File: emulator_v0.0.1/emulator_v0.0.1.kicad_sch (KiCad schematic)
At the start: 11 parts, among them J1 Conn_01x10_Socket, J2 Conn_01x05_Pin, U1 L7805

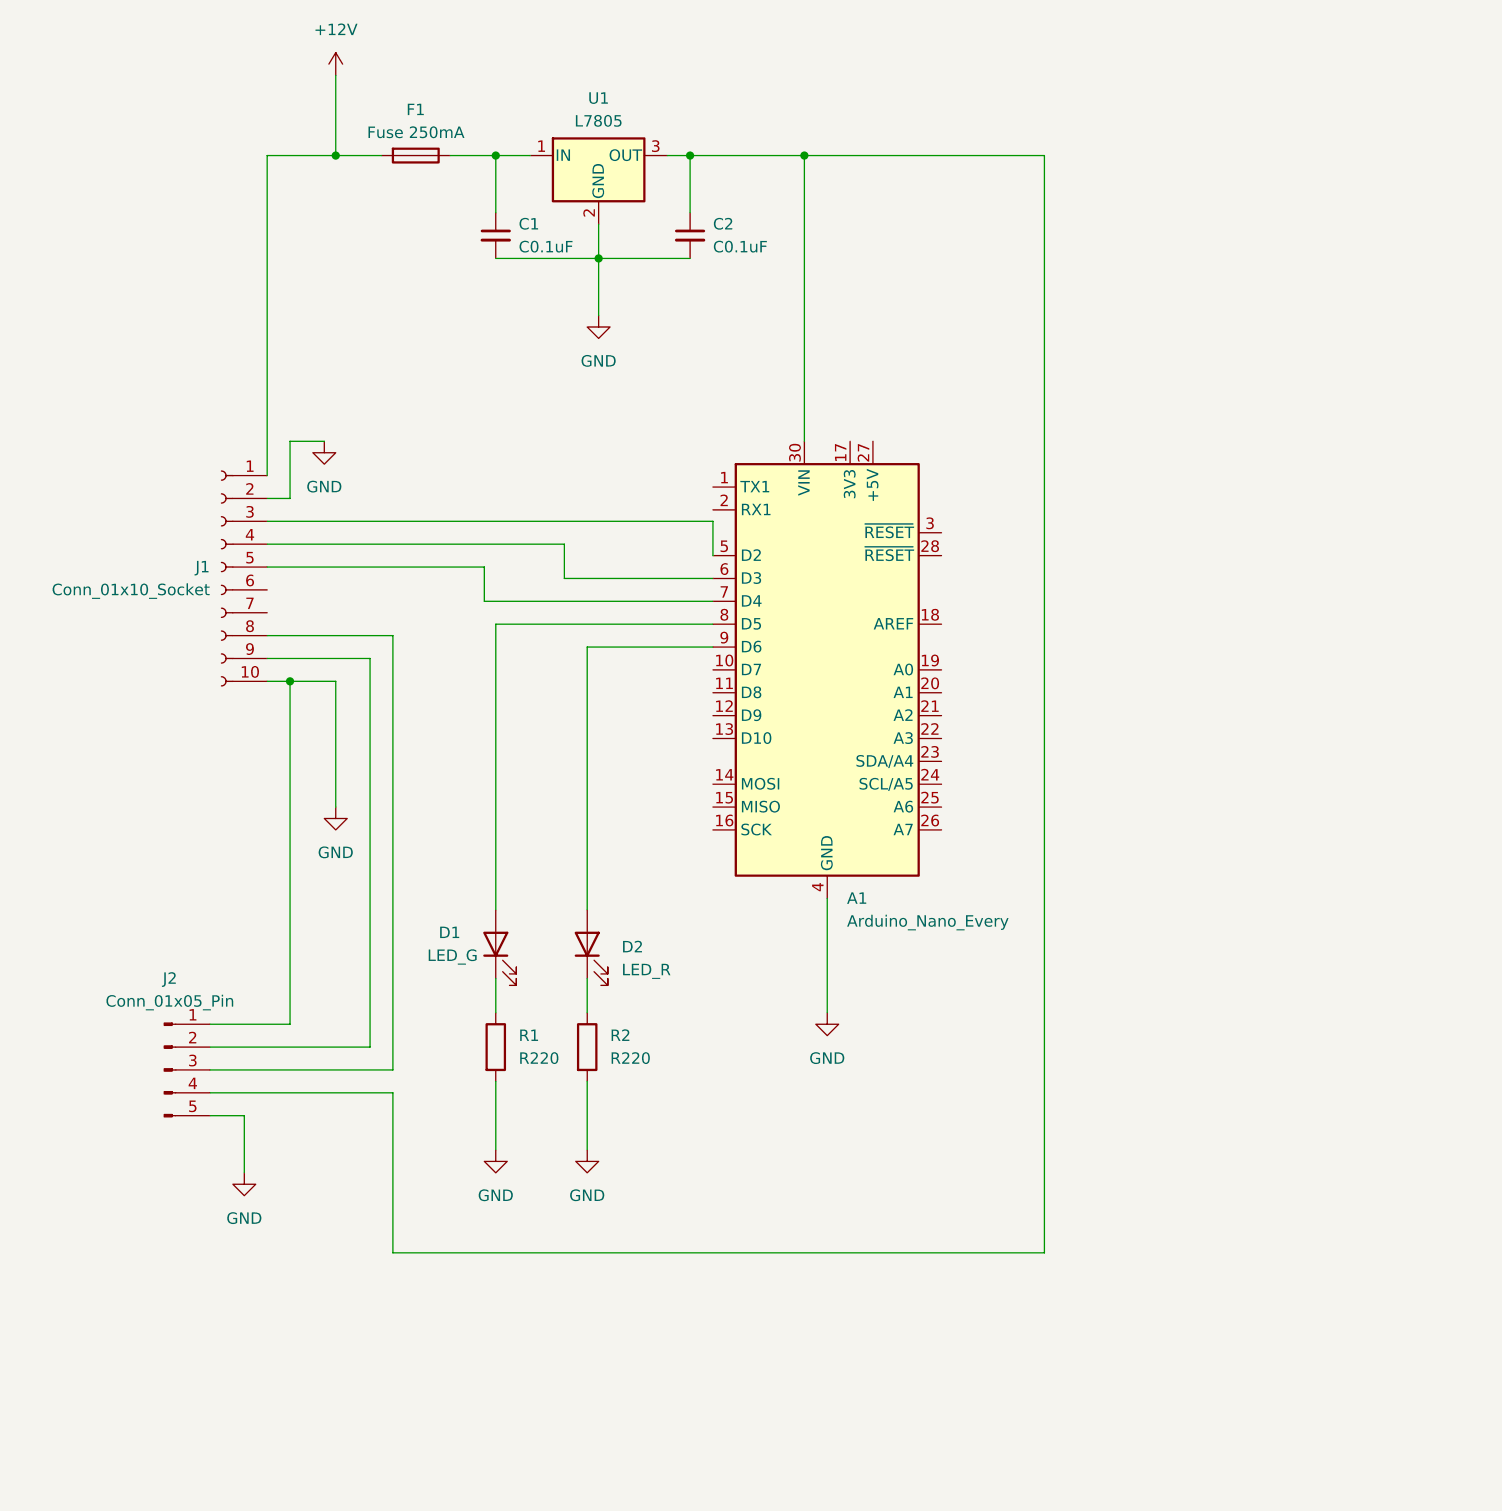
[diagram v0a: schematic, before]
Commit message: added control for powering up
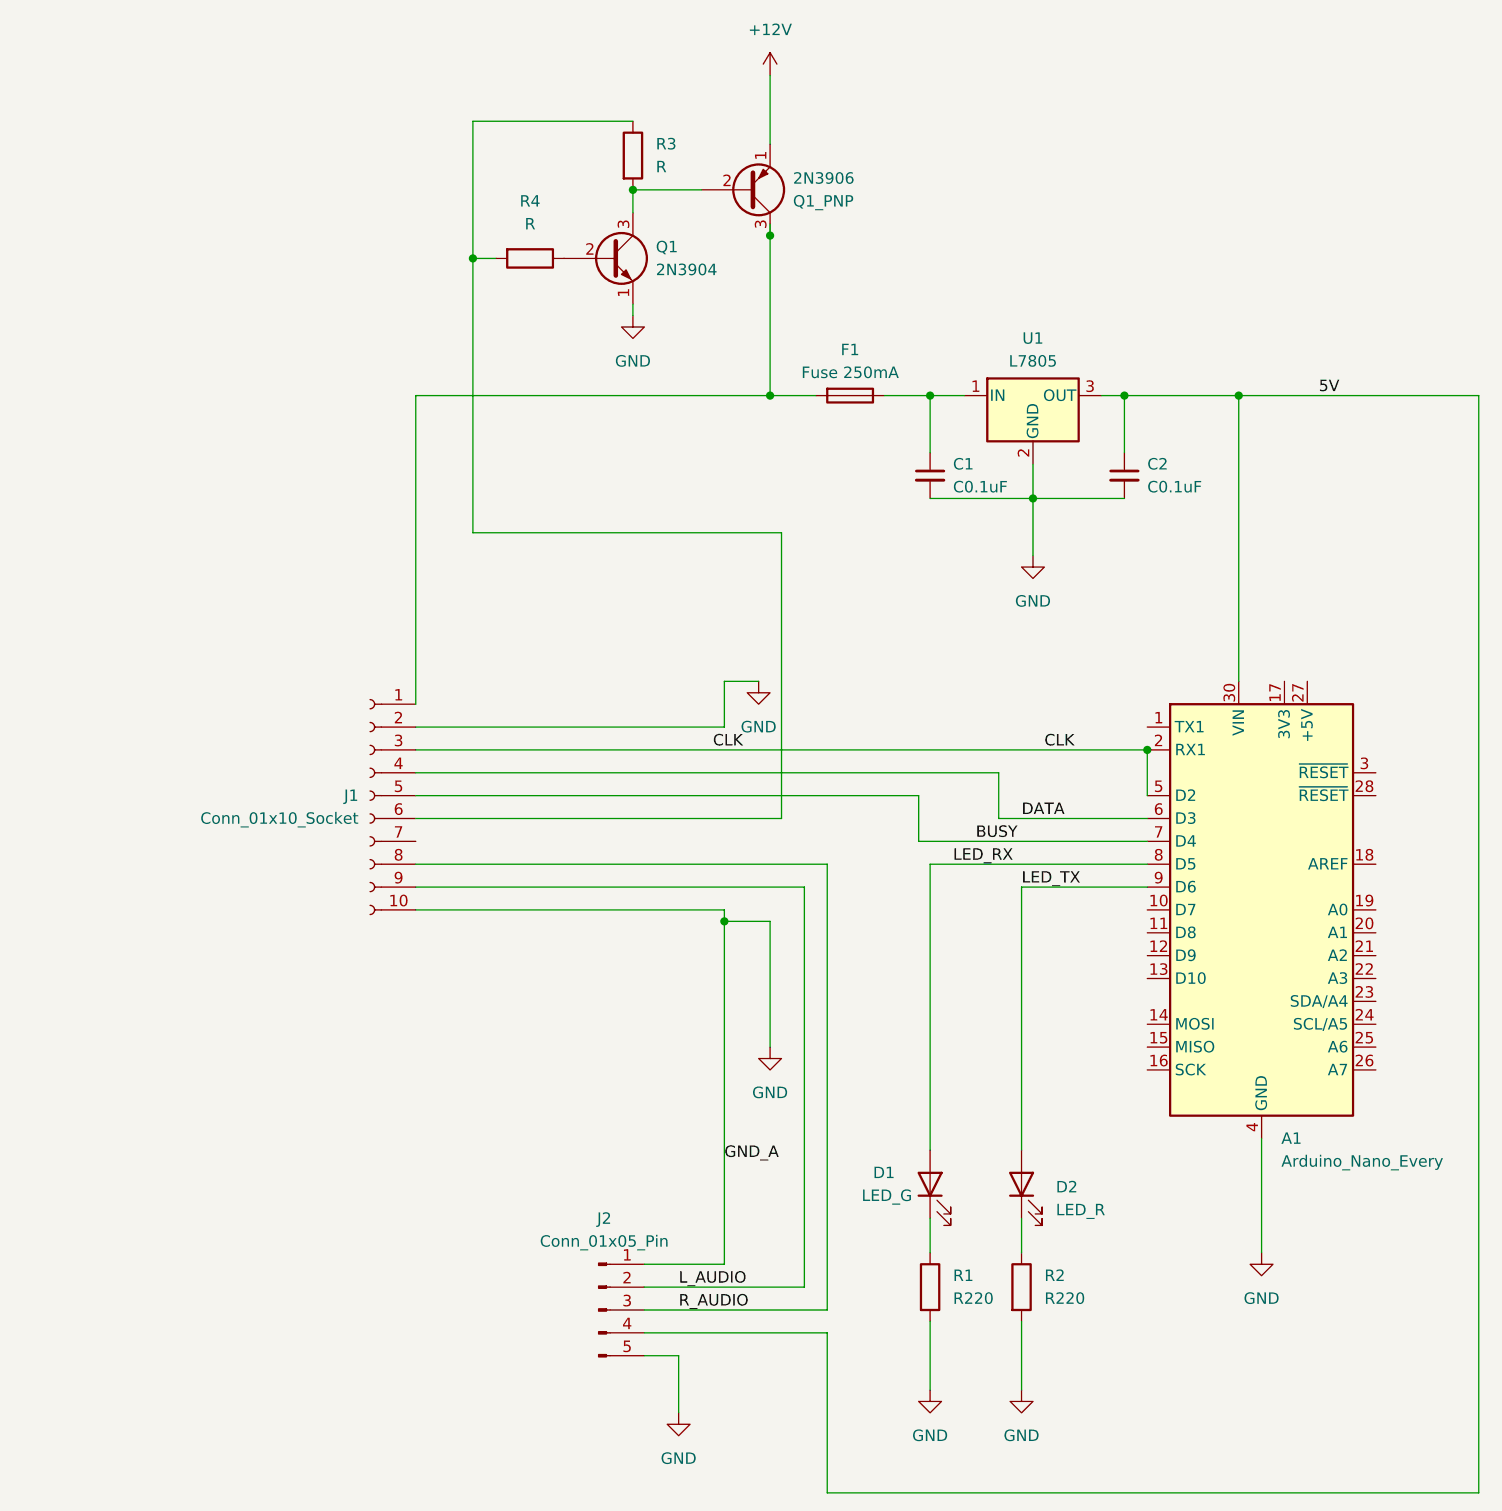
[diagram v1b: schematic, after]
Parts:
- added Q1: 2N3904, Package_TO_SOT_THT:TO-92_Inline, symbol Transistor_BJT:2N3904
- added Q1_PNP: 2N3906, Package_TO_SOT_THT:TO-92_Inline, symbol Transistor_BJT:2N3906
- added R3, R4: R, symbol Device:R
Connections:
- net +12V: now also Q1_PNP.1 (E); no longer F1.2, J1.1 (Pin_1)
- net GND: now also Q1.1 (E)
- net LED_TX: now reaches A1.9 (D6), D2.2 (A)
- net 5V: now reaches A1.30 (VIN), C2.1, J2.4 (Pin_4), U1.3 (OUT)
- net CLK: now reaches A1.5 (D2), J1.3 (Pin_3)
- net CLK: now also A1.2 (RX1)
- net DATA: now reaches A1.6 (D3), J1.4 (Pin_4)
- net BUSY: now reaches A1.7 (D4), J1.5 (Pin_5)
- net at J1.6 (Pin_6): now also R3.1, R4.2
- net R_AUDIO: now reaches J1.8 (Pin_8), J2.3 (Pin_3)
- net L_AUDIO: now reaches J1.9 (Pin_9), J2.2 (Pin_2)
- net LED_RX: now reaches A1.8 (D5), D1.2 (A)
- new net: Q1.2 (B), R4.1
- new net: Q1.3 (C), Q1_PNP.2 (B), R3.2
- new net: F1.2, J1.1 (Pin_1), Q1_PNP.3 (C)
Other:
- moved on the sheet: A1, C1, C2, D1, D2, F1, J1, J2, R1, R2, U1
